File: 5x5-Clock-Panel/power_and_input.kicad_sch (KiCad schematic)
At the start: 0 parts

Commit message: startet work on power and connectors
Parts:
- added C1: C, symbol Device:C
- added C2: C_Polarized, symbol Device:C_Polarized
- added D1, D2, D3, D4, D5, D6: D_TVS, symbol Device:D_TVS
- added F1: Fuse, symbol Device:Fuse
- added J1: Conn_01x02_Socket, symbol Connector:Conn_01x02_Socket
- added J2: Conn_01x04_Socket, symbol Connector:Conn_01x04_Socket
- added L1: L_Coupled, symbol Device:L_Coupled
- added R1, R2, R3, R4: R, symbol Device:R
- added RV1: Varistor, symbol Device:Varistor
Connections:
- new net: D3.2 (A2), D6.2 (A2), J2.3 (Pin_3), R3.1
- new net: D4.2 (A2), D6.1 (A1), J2.4 (Pin_4), R4.1
- new net: F1.1, J1.1 (Pin_1)
- new net: J1.2 (Pin_2), L1.3, RV1.2
- new net: F1.2, L1.1, RV1.1
- new net +5V: C1.1, C2.1, L1.2
- new net GND: C1.2, C2.2, D1.1 (A1), D2.1 (A1), D3.1 (A1), D4.1 (A1), L1.4
- new net RS485_RX+_R1: D1.2 (A2), D5.2 (A2), J2.1 (Pin_1), R1.1
- new net RS485_RX-_R2: D2.2 (A2), D5.1 (A1), J2.2 (Pin_2), R2.1

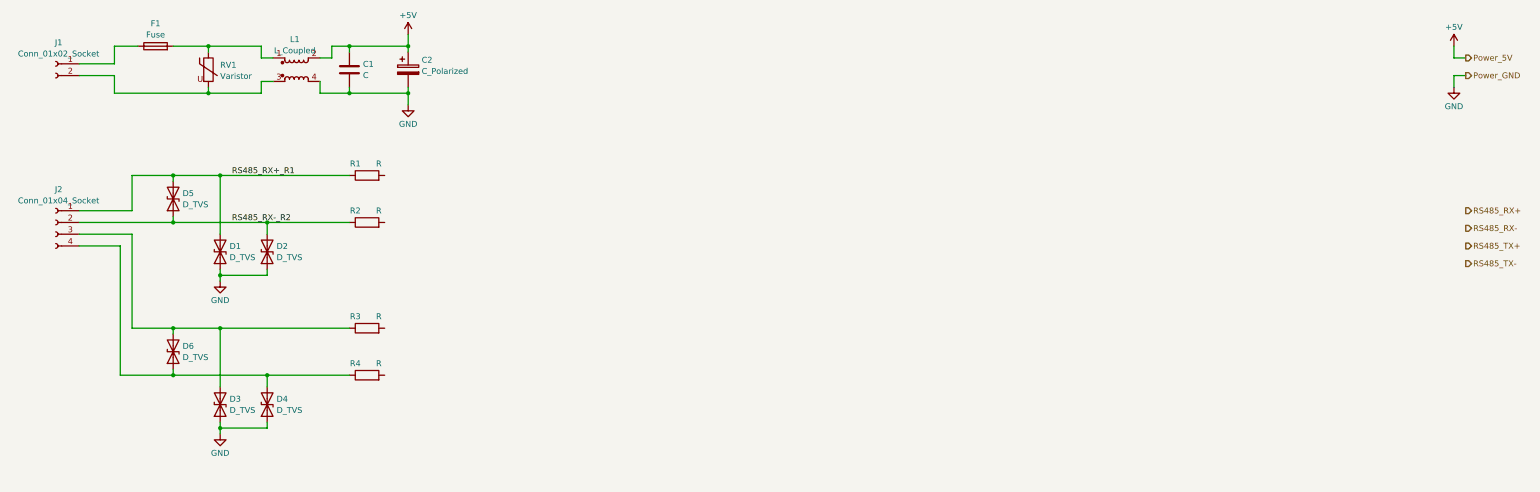
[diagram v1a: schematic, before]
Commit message: added rs485 tranceiver
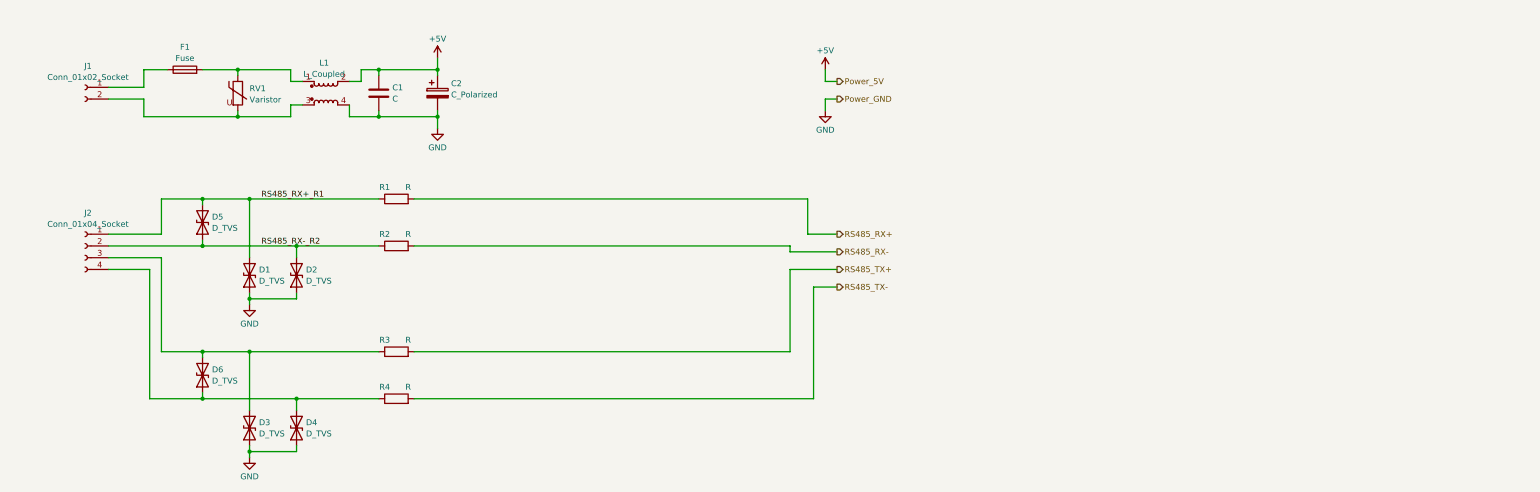
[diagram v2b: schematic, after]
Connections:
- net RS485_RX+: now also R1.2
- net RS485_RX-: now also R2.2
- net RS485_TX+: now also R3.2
- net RS485_TX-: now also R4.2
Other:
- moved on the sheet: C1, C2, D1, D2, D3, D4, D5, D6, F1, J1, J2, L1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
